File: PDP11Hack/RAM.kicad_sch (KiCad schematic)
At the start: 9 parts, among them U21 74HCT139, U28 AS6C4008-55PCN, U29 AS6C4008-55PCN

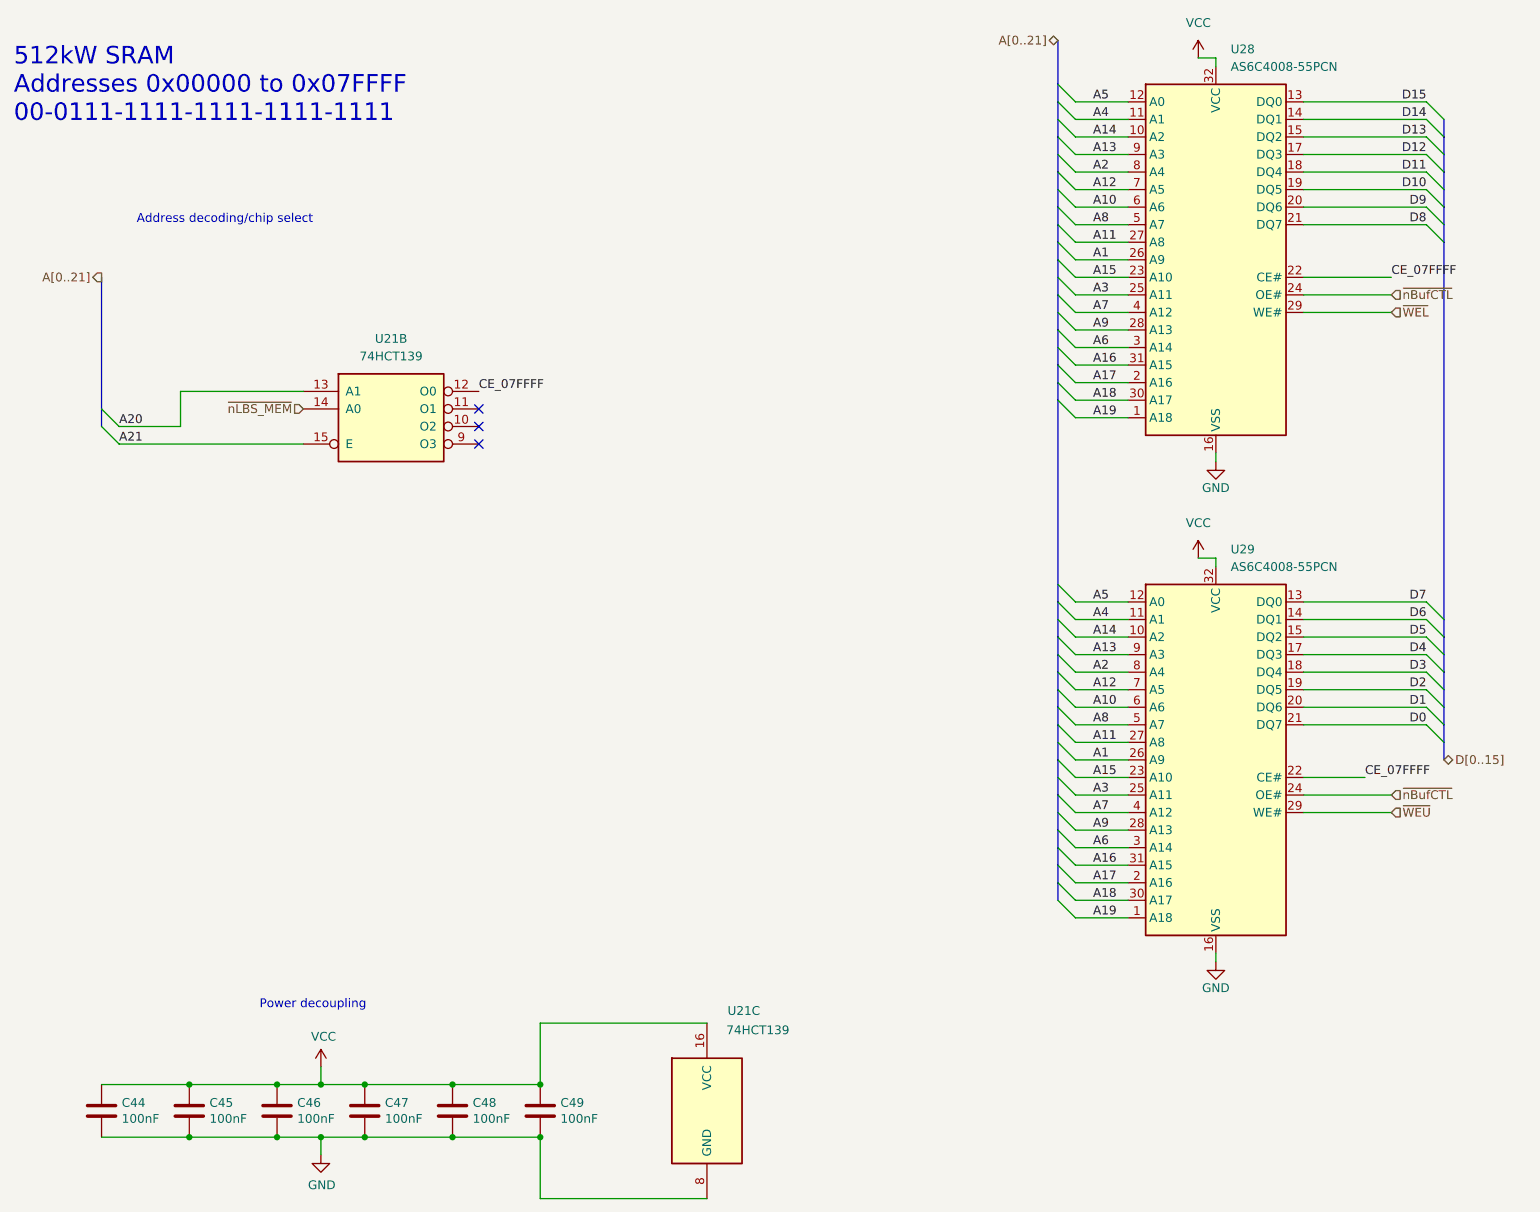
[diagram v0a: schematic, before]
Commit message: Corrections thanks to Peter Schranz on VCFED
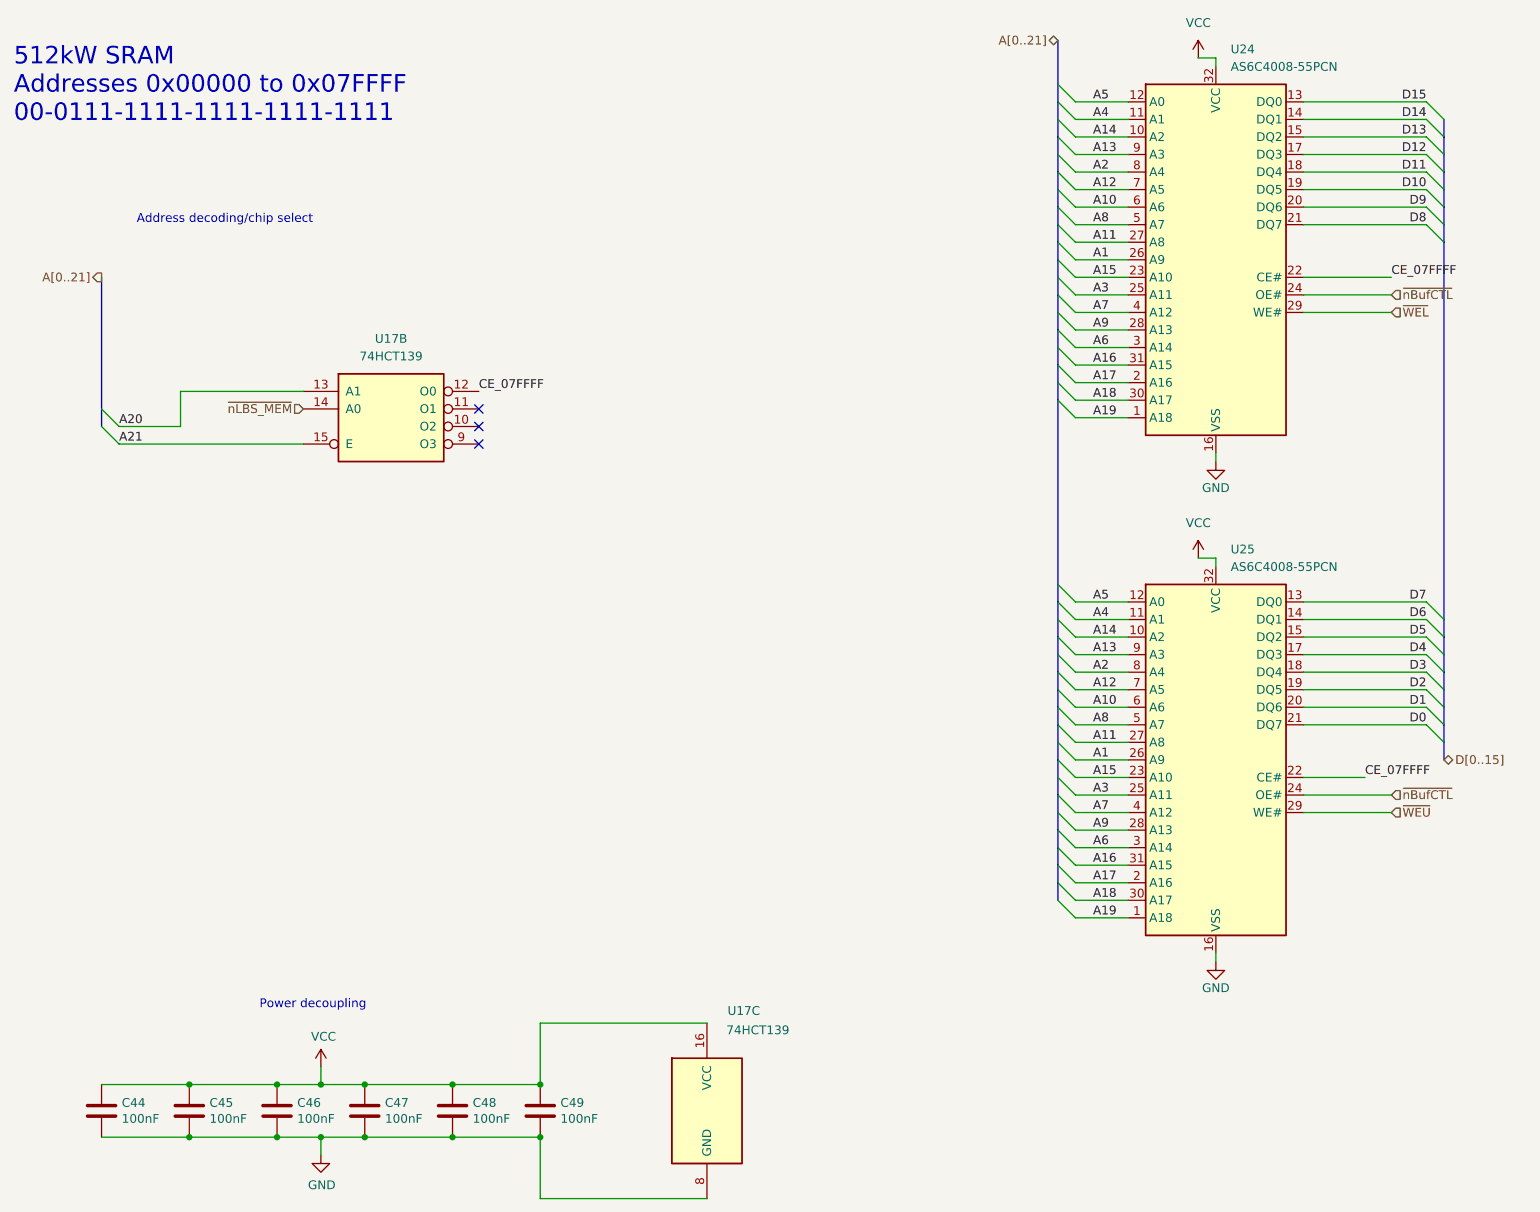
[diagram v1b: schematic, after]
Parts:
- renumbered U21 to U17, U28 to U24, U29 to U25
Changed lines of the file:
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@@
 		(dnp no)
 		(fields_autoplaced yes)
-		(property "Reference" "U28"
+		(property "Reference" "U24"
 			(at 209.1533 20.32 0)
 			(effects
@@
 			(project "Modular DCJ11"
 				(path "/264d9b66-53d1-4564-94e8-42c7c0bb6a66/8011c564-4a76-4fb5-92ec-d9b18aa7105f"
-					(reference "U28")
+					(reference "U24")
 					(unit 1)
 				)
@@
 		(on_board yes)
 		(dnp no)
-		(property "Reference" "#PWR079"
+		(property "Reference" "#PWR080"
 			(at 207.01 158.75 0)
 			(effects
@@
 			(project "Modular DCJ11"
 				(path "/264d9b66-53d1-4564-94e8-42c7c0bb6a66/8011c564-4a76-4fb5-92ec-d9b18aa7105f"
-					(reference "#PWR079")
+					(reference "#PWR080")
 					(unit 1)
 				)
@@
 		(on_board yes)
 		(dnp no)
-		(property "Reference" "#PWR077"
+		(property "Reference" "#PWR078"
 			(at 204.47 97.79 0)
 			(effects
@@
 			(project "Modular DCJ11"
 				(path "/264d9b66-53d1-4564-94e8-42c7c0bb6a66/8011c564-4a76-4fb5-92ec-d9b18aa7105f"
-					(reference "#PWR077")
+					(reference "#PWR078")
 					(unit 1)
 				)
@@
 		(on_board yes)
 		(dnp no)
-		(property "Reference" "#PWR073"
+		(property "Reference" "#PWR076"
 			(at 77.47 186.69 0)
 			(effects
@@
 			(project "Modular DCJ11"
 				(path "/264d9b66-53d1-4564-94e8-42c7c0bb6a66/8011c564-4a76-4fb5-92ec-d9b18aa7105f"
-					(reference "#PWR073")
+					(reference "#PWR076")
 					(unit 1)
 				)
@@
 		(on_board yes)
 		(dnp no)
-		(property "Reference" "#PWR072"
+		(property "Reference" "#PWR075"
 			(at 77.47 171.45 0)
 			(effects
@@
 			(project "Modular DCJ11"
 				(path "/264d9b66-53d1-4564-94e8-42c7c0bb6a66/8011c564-4a76-4fb5-92ec-d9b18aa7105f"
-					(reference "#PWR072")
+					(reference "#PWR075")
 					(unit 1)
 				)
@@
 		(dnp no)
 		(fields_autoplaced yes)
-		(property "Reference" "U29"
+		(property "Reference" "U25"
 			(at 209.1533 92.71 0)
 			(effects
@@
 			(project "Modular DCJ11"
 				(path "/264d9b66-53d1-4564-94e8-42c7c0bb6a66/8011c564-4a76-4fb5-92ec-d9b18aa7105f"
-					(reference "U29")
+					(reference "U25")
 					(unit 1)
 				)
@@
 		(dnp no)
 		(fields_autoplaced yes)
-		(property "Reference" "U21"
+		(property "Reference" "U17"
 			(at 87.63 62.23 0)
 			(effects
@@
 			(project "Modular DCJ11"
 				(path "/264d9b66-53d1-4564-94e8-42c7c0bb6a66/8011c564-4a76-4fb5-92ec-d9b18aa7105f"
-					(reference "U21")
+					(reference "U17")
 					(unit 2)
 				)
@@
 		(on_board yes)
 		(dnp no)
-		(property "Reference" "U21"
+		(property "Reference" "U17"
 			(at 138.684 159.512 0)
 			(effects
@@
 			(project "Modular DCJ11"
 				(path "/264d9b66-53d1-4564-94e8-42c7c0bb6a66/8011c564-4a76-4fb5-92ec-d9b18aa7105f"
-					(reference "U21")
+					(reference "U17")
 					(unit 3)
 				)
@@
 		(on_board yes)
 		(dnp no)
-		(property "Reference" "#PWR078"
+		(property "Reference" "#PWR079"
 			(at 207.01 86.36 0)
 			(effects
@@
 			(project "Modular DCJ11"
 				(path "/264d9b66-53d1-4564-94e8-42c7c0bb6a66/8011c564-4a76-4fb5-92ec-d9b18aa7105f"
-					(reference "#PWR078")
+					(reference "#PWR079")
 					(unit 1)
 				)
@@
 		(on_board yes)
 		(dnp no)
-		(property "Reference" "#PWR076"
+		(property "Reference" "#PWR077"
 			(at 204.47 25.4 0)
 			(effects
@@
 			(project "Modular DCJ11"
 				(path "/264d9b66-53d1-4564-94e8-42c7c0bb6a66/8011c564-4a76-4fb5-92ec-d9b18aa7105f"
-					(reference "#PWR076")
-					(unit 1)
-				)
+					(reference "#PWR077")
+					(unit 1)
+				)

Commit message: Last update, PCB creation ready
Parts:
- U17: footprint (none) -> Package_DIP:DIP-16_W7.62mm
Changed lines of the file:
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@@
 			)
 		)
-		(property "Footprint" ""
+		(property "Footprint" "Package_DIP:DIP-16_W7.62mm"
 			(at 87.63 72.39 0)
 			(effects
@@
 			)
 		)
-		(property "Footprint" ""
+		(property "Footprint" "Package_DIP:DIP-16_W7.62mm"
 			(at 133.35 173.99 0)
 			(effects
